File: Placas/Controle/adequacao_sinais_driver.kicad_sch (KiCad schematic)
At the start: 0 parts

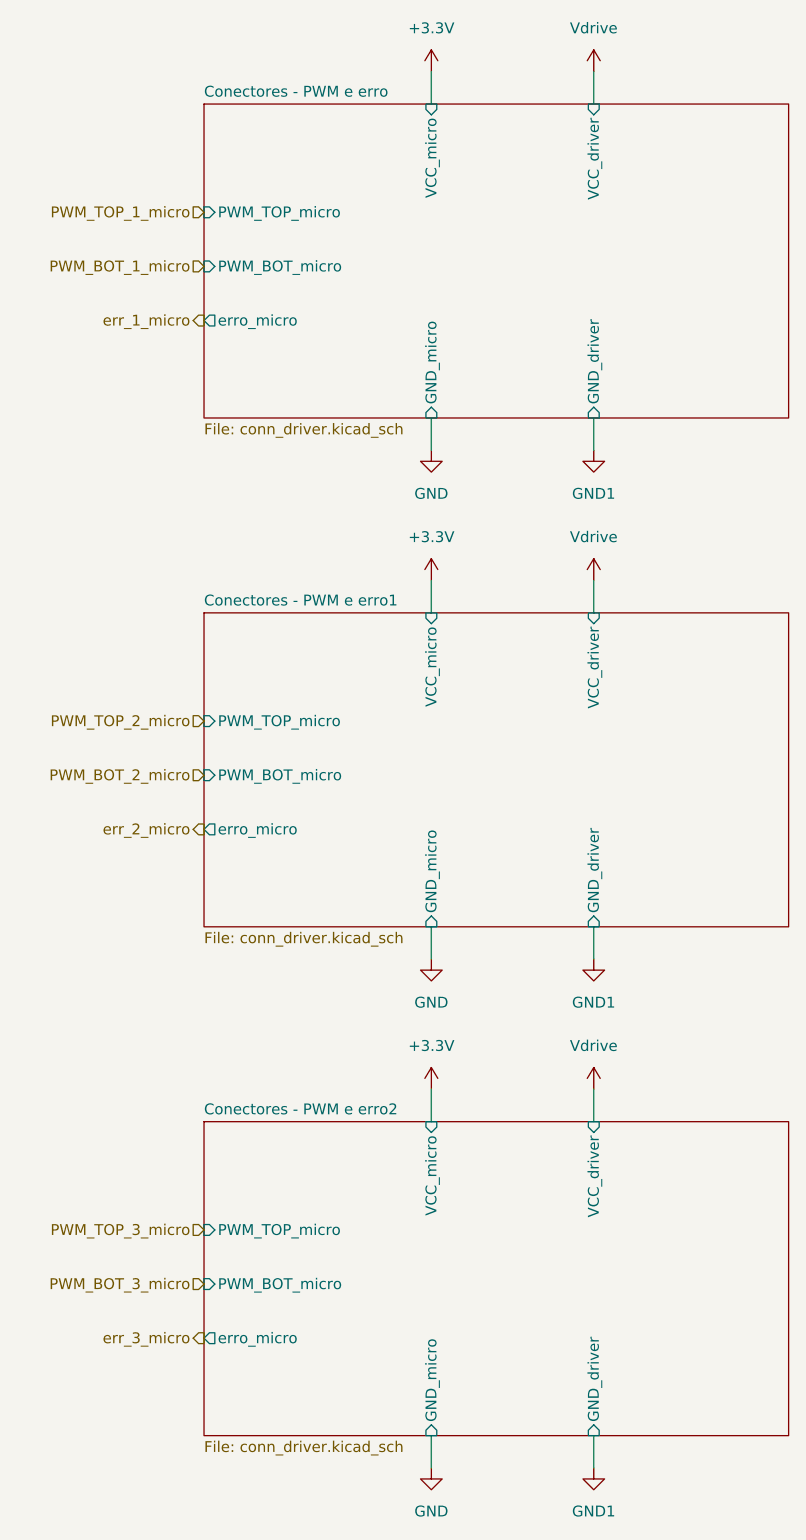
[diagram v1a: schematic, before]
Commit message: Modificações nas duas placas, adição de furos para montagem, melhora na posição dos micros e conectores para comunicação SPI
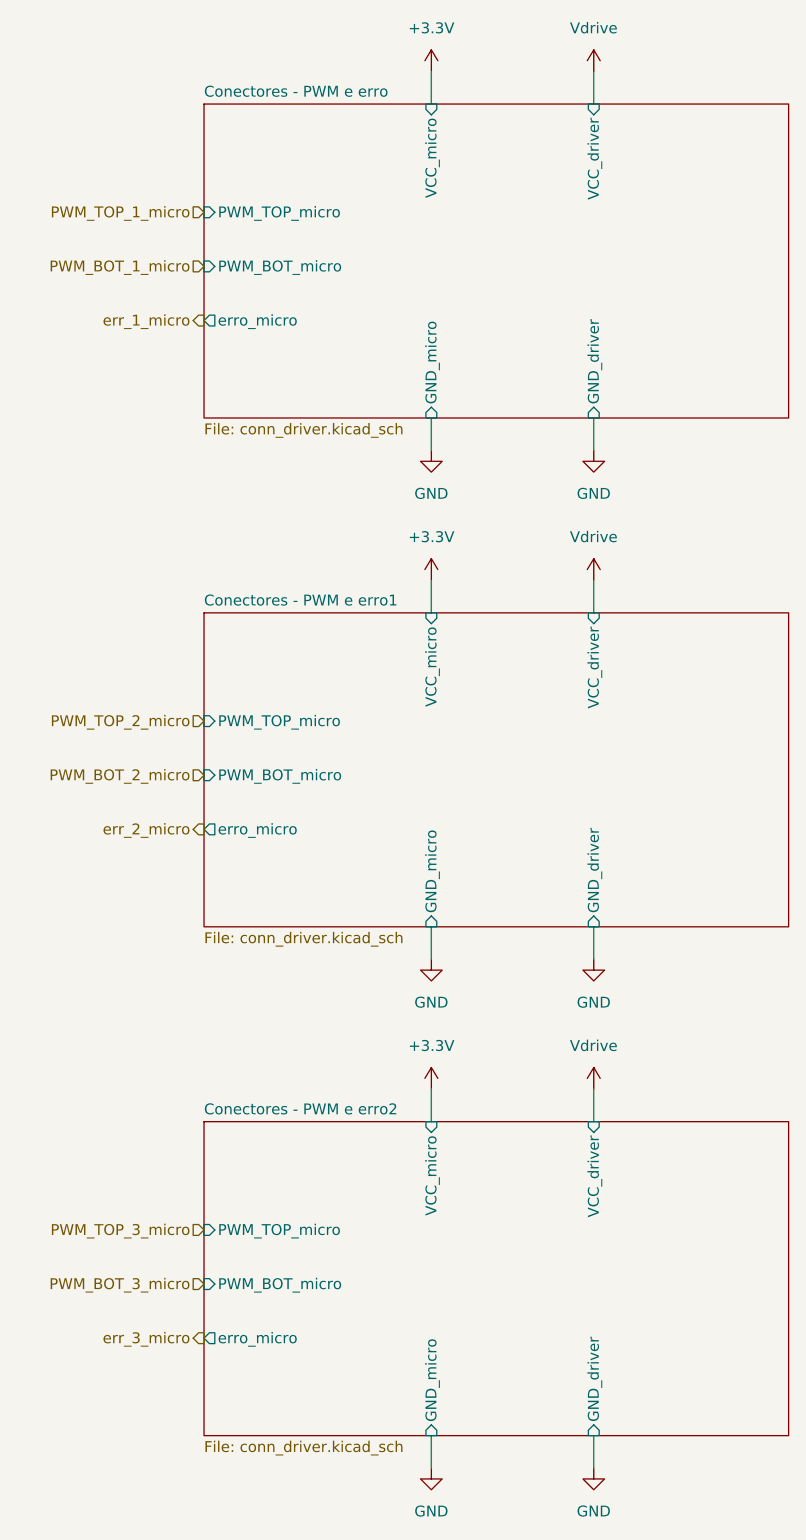
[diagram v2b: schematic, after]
